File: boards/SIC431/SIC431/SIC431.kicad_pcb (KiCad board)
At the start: 2 copper layers, 127 x 127 mm, 95 parts, among them J101 Screw_Terminal_01x02, J102 Screw_Terminal_01x06, J103 Screw_Terminal_01x06, J104 Screw_Terminal_01x06, J105 Conn_02x02_Top_Bottom, J106 Conn_02x02_Top_Bottom, J107 Conn_02x02_Top_Bottom, J108 Screw_Terminal_01x02, J109 Screw_Terminal_01x02, J110 Screw_Terminal_01x02, K101 Relay, K102 Relay, K103 Relay, K104 Relay, K105 Relay, K106 Relay, SW101 SW_Push_Open, U101 SIC431AED-T1-GE3, U102 SIC431AED-T1-GE3, U103 SIC431AED-T1-GE3

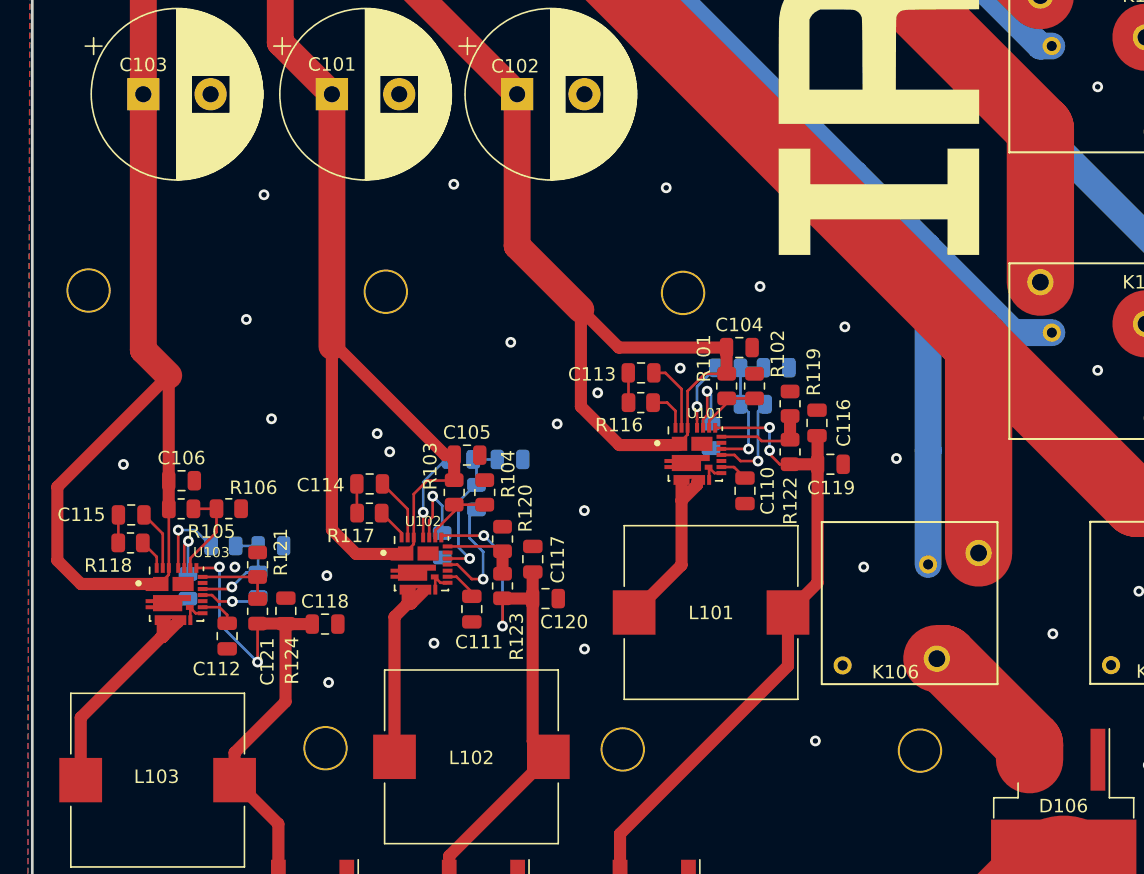
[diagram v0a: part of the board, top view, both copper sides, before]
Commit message: update 5v backup regulator footprint
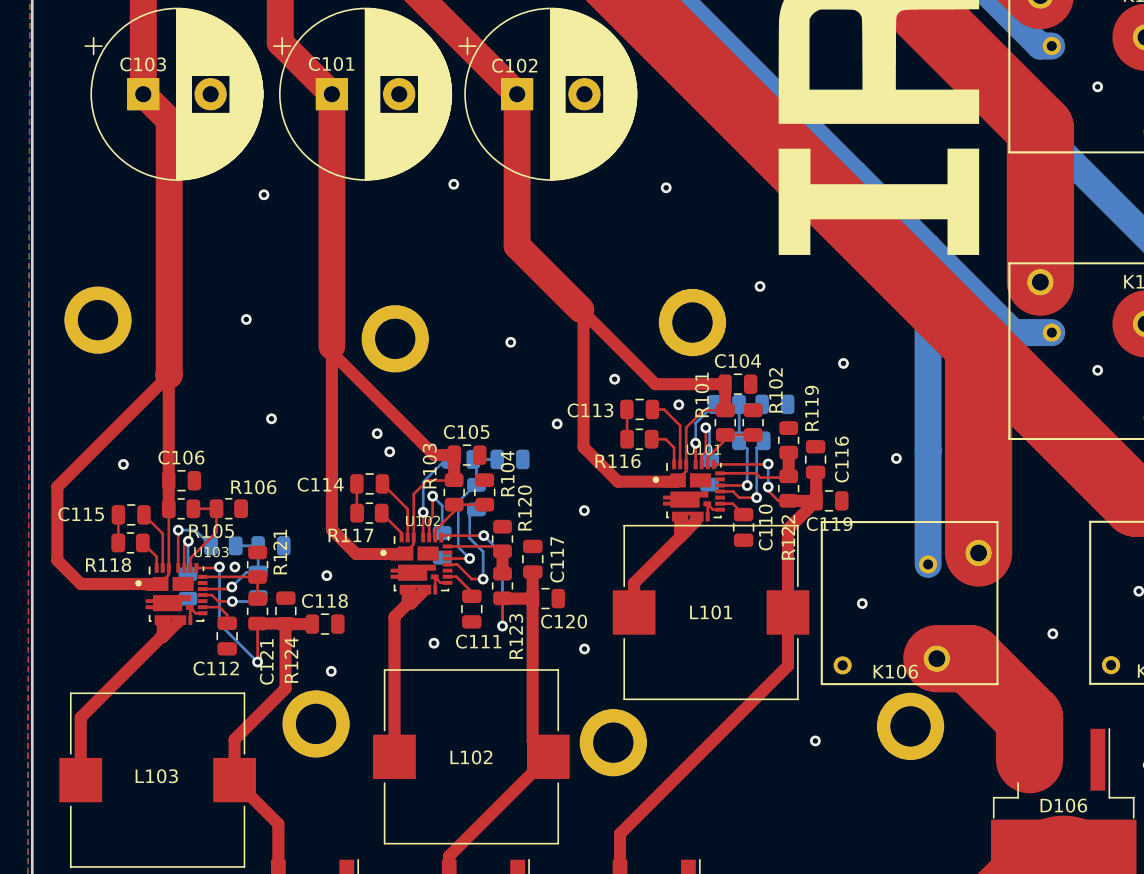
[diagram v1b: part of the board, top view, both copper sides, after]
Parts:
- moved C107 2.72 mm to (75.2, 82.5)
- moved C116 2.72 mm to (78.2, 86.6)
- moved R102 2.72 mm to (73.5, 83.8)
- moved R116 2.72 mm to (65.1, 85.0)
- moved R119 2.72 mm to (76.2, 85.1)
- moved C104 2.72 mm to (72.4, 81.0)
- moved C110 2.72 mm to (72.8, 91.6)
- moved C113 2.72 mm to (65.1, 82.8)
- moved C119 2.72 mm to (79.2, 89.6)
- moved R101 2.72 mm to (71.5, 83.8)
- moved R107 2.72 mm to (71.6, 82.5)
- moved R110 2.72 mm to (73.4, 85.2)
- moved R113 2.72 mm to (70.3, 87.5)
- moved U101 2.72 mm to (69.2, 88.9)
- moved R122 2.72 mm to (76.2, 88.7)
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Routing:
- net /V_BAT_IN: track 492.7 -> 496.2 mm
- net Net-(C116-Pad1): track 49.9 -> 47.1 mm
- net Net-(L101-Pad1): track 13.0 -> 11.0 mm
- net Net-(D106-Pad1): track 10.7 -> 11.8 mm
